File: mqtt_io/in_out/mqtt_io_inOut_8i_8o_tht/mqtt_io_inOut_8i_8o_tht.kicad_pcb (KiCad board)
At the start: 2 copper layers, 162.6 x 134.6 mm, 109 parts, among them J13 Conn_01x02, J3 Conn_01x04_Pin, J4 Conn_01x04_Pin, K1 FINDER-40.31, K2 FINDER-40.31, K3 FINDER-40.31, K4 FINDER-40.31, K5 FINDER-40.31, K6 FINDER-40.31, K7 FINDER-40.31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

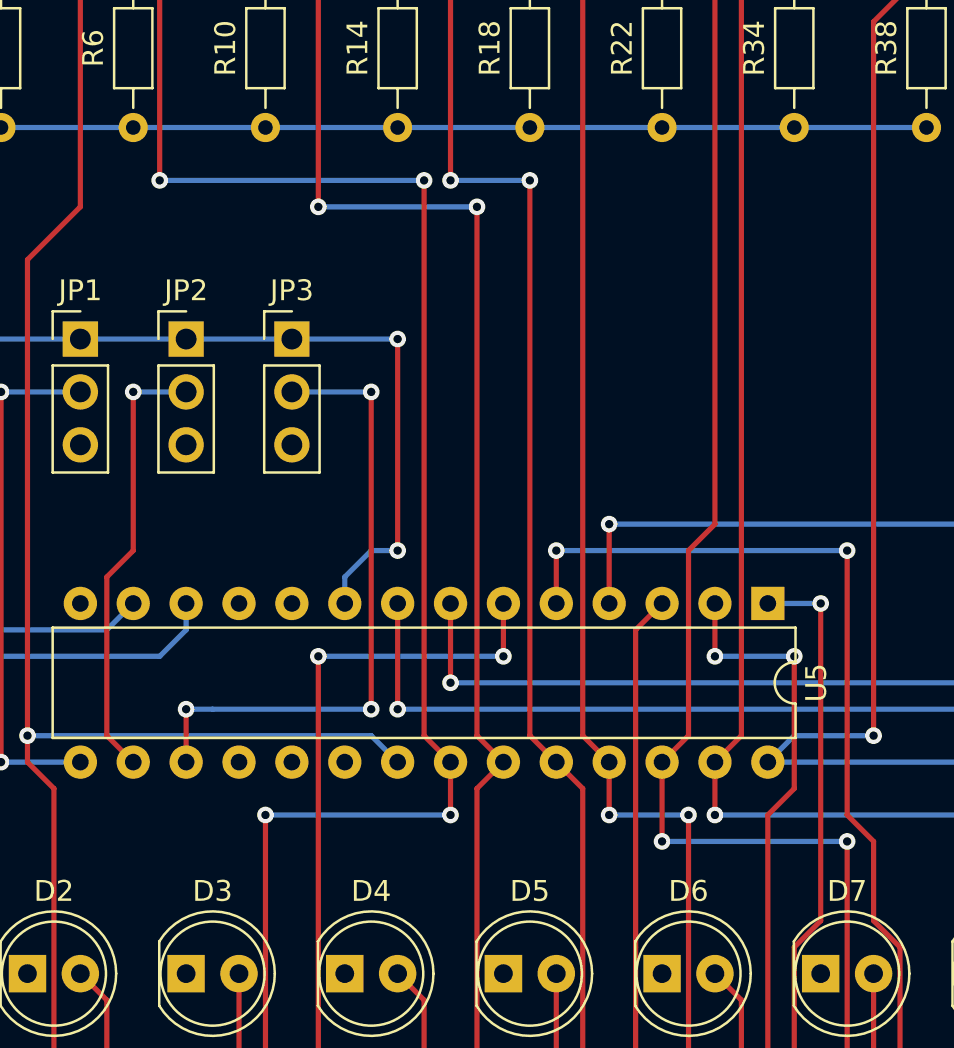
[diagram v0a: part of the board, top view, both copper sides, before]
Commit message: Pullup für ic2 eingefügt (4k7)
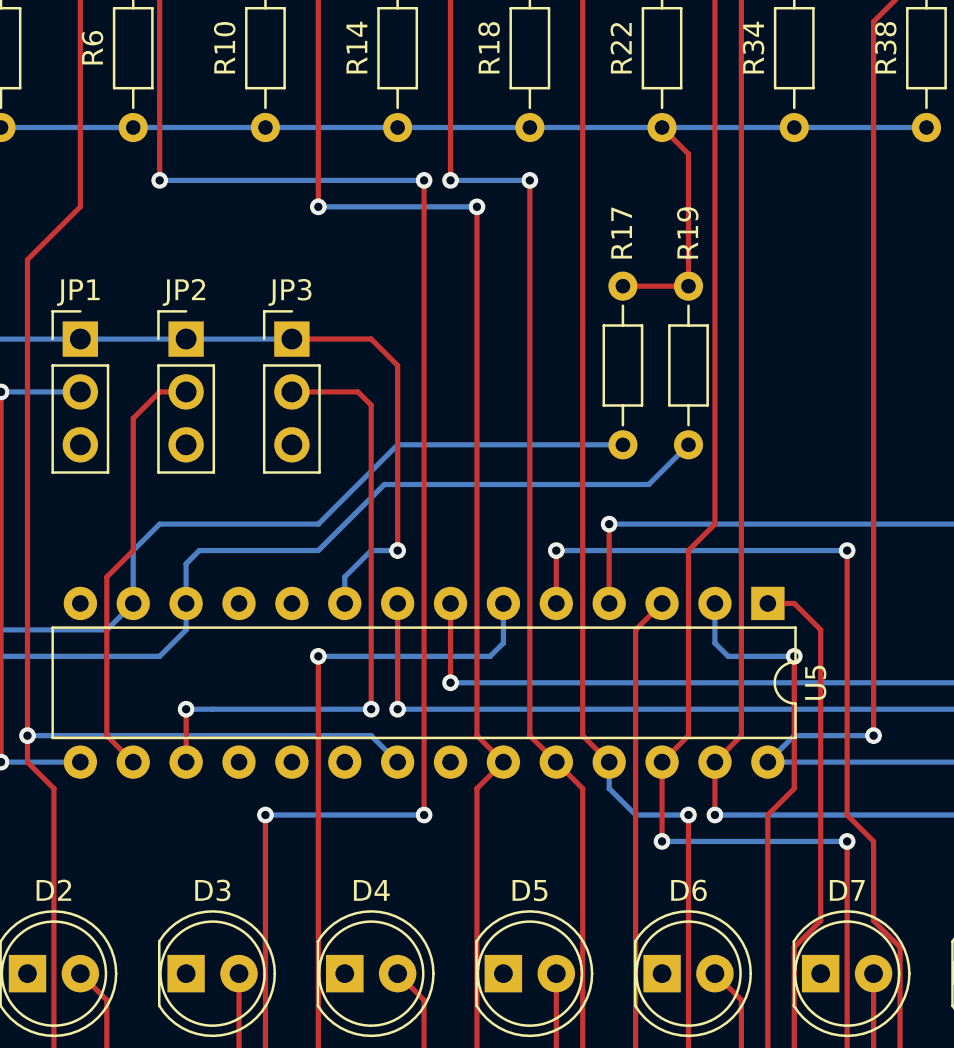
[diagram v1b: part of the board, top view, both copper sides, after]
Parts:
- added R17: 4k7, Resistor_THT:R_Axial_DIN0204_L3.6mm_D1.6mm_P7.62mm_Horizontal, F.Cu at (54.0, 76.2)
- added R19: 4k7, Resistor_THT:R_Axial_DIN0204_L3.6mm_D1.6mm_P7.62mm_Horizontal, F.Cu at (57.1, 76.2)
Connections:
- U5 pad 22: /a1 -> unconnected-(U5-GPA1-Pad22)
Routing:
- net Net-(J3-Pin_3): track 47.5 -> 75.9 mm
- net Net-(J3-Pin_2): track 43.7 -> 71.9 mm
- net +5V: track 107.7 -> 118.3 mm, vias 5 -> 4
- net /a1: track 84.9 -> 83.1 mm
- net /a4: track 65.8 -> 65.1 mm, vias 3 -> 2
- net /AD1: track 21.4 -> 20.6 mm, vias 1 -> 0
- net /b0: track 131.4 -> 130.7 mm, vias 4 -> 3
- net /b1: track 138.7 -> 138.4 mm, vias 6 -> 5
- net /AD2: track 30.5 -> 30.1 mm, vias 3 -> 2
- net /b5: track 145.1 -> 144.7 mm, vias 6 -> 5

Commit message: neue Dateien eingefügt.
out Platine rev 2, testprogramm für pi pico
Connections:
- J3 pad 1: +5V -> VDD
- J4 pad 1: +5V -> VDD
- JP1 pad 1: +5V -> VDD
- JP2 pad 1: +5V -> VDD
- JP3 pad 1: +5V -> VDD
- R10 pad 1: +5V -> VDD
- R14 pad 1: +5V -> VDD
- R17 pad 2: +5V -> VDD
- R18 pad 1: +5V -> VDD
- R19 pad 2: +5V -> VDD
- R2 pad 1: +5V -> VDD
- R22 pad 1: +5V -> VDD
- R34 pad 1: +5V -> VDD
- R38 pad 1: +5V -> VDD
- R6 pad 1: +5V -> VDD
- U5 pad 18: GND -> VDD
- U5 pad 22: unconnected-(U5-GPA1-Pad22) -> /a1
- U5 pad 9: +5V -> VDD
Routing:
- net VDD: track 0.00 -> 129.0 mm, vias 0 -> 2
- net +5V: track 118.3 -> 0.00 mm, vias 4 -> 0
- net /a1: track 83.1 -> 85.8 mm, vias 5 -> 4
- net /a3: track 69.6 -> 67.4 mm, vias 4 -> 0
- net /b4: track 120.0 -> 117.8 mm, vias 4 -> 1
- net /b5: track 144.7 -> 146.1 mm
- net Net-(J3-Pin_2): track 71.9 -> 71.1 mm, vias 3 -> 2
- net /b7: track 163.6 -> 162.9 mm, vias 3 -> 2
- net /a6: track 78.5 -> 77.8 mm, vias 3 -> 2
- net /a5: track 74.0 -> 73.2 mm, vias 3 -> 2
- net /a2: track 73.4 -> 72.7 mm, vias 4 -> 3
- net /a4: track 65.1 -> 64.3 mm, vias 2 -> 1
- net /a0: track 82.6 -> 81.9 mm, vias 2 -> 1
- net /b6: track 146.1 -> 145.8 mm, vias 3 -> 2
